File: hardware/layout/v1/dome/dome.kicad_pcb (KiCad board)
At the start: 4 copper layers, 13.6 x 13.6 mm, 5 parts, among them J1 CROWN_RISER, U1 LTR-390UV-01, U2 VEML7700-TT

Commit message: Update documentation to reflect hardware specification changes and component substitutions
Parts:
- moved C2 8.42 mm to (6.80, -2.10)
- moved C1 2.64 mm to (6.80, -11.5)
- moved J1 1.30 mm to (6.80, -6.80)
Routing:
- net I2C_SCL: track 8.54 -> 11.1 mm
- net I2C_SDA: track 11.5 -> 13.3 mm, vias 2 -> 1
- net GND: track 17.9 -> 16.3 mm
- net +3V3: track 20.0 -> 19.5 mm

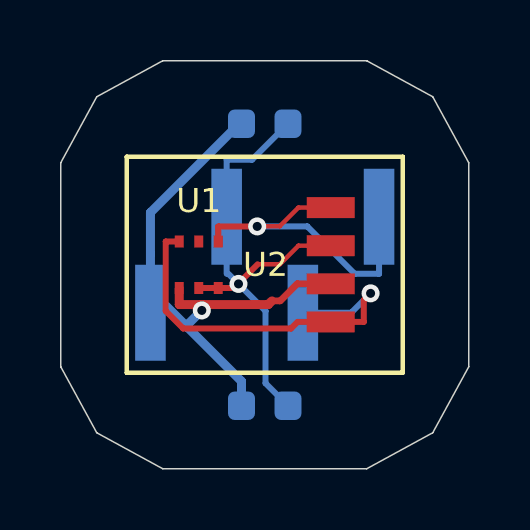
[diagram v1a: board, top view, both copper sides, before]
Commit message: Redesign crown PCB
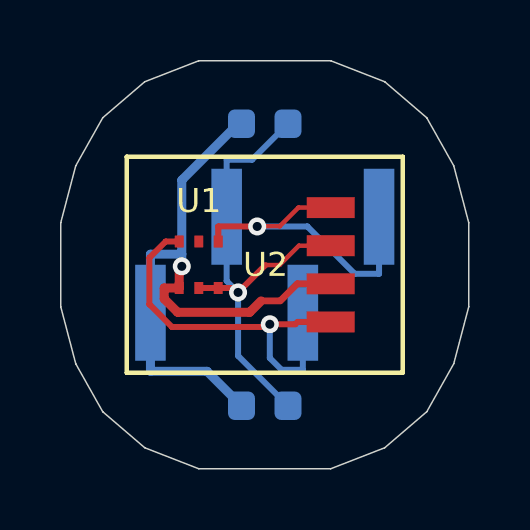
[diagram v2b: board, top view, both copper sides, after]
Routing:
- net +3V3: track 19.5 -> 21.9 mm
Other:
- outline, holes or cut-outs redrawn

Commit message: Add silkscreen connector labels to all PCB variants for improved assembly identification
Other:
- board text added: "CROWN"

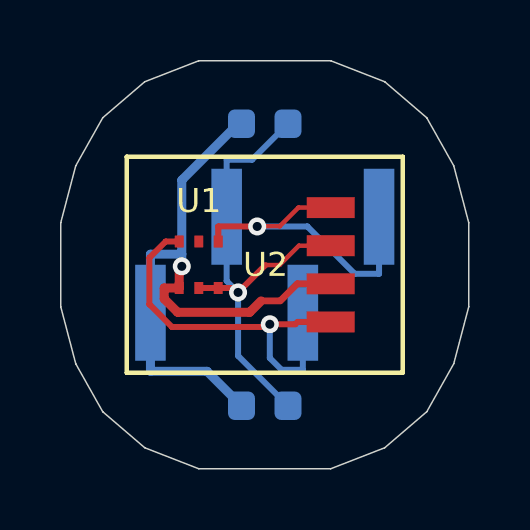
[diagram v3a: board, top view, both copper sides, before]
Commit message: Upgrade dome PCB with enhanced light sensing capabilities: add TSL25911FN visible/NIR sensor and optional GUVB-C31SM UV-B sensor
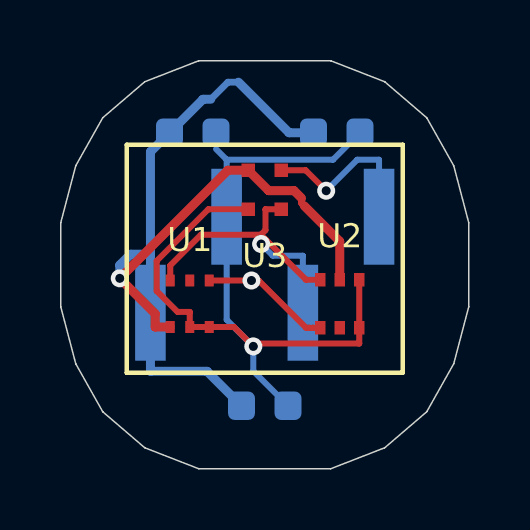
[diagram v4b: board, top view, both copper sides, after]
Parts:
- added C3: 100n 50V, Capacitor_SMD:C_0603_1608Metric, B.Cu at (6.80, -2.10)
- added U3: GUVB-C31SM, gateway_fp:GenUV_GUVB-C31SM, F.Cu at (6.80, -9.30)
- U2: value VEML7700-TT -> TSL25911FN; footprint gateway_fp:Vishay_VEML7700-TT -> gateway_fp:AMS_TSL25911FN
- moved C2 9.41 mm to (9.20, -11.2)
- moved C1 2.42 mm to (4.40, -11.2)
- moved U1 1.33 mm to (4.30, -5.50)
- moved U2 1.33 mm to (9.30, -5.50), turned to 0 degrees
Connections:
- U2 pad 1: I2C_SDA -> I2C_SCL
- U2 pad 2: +3V3 -> (no net)
- U2 pad 4: I2C_SCL -> GND
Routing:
- net GND: track 16.5 -> 29.0 mm
- net +3V3: track 21.9 -> 33.3 mm
- net I2C_SCL: track 11.1 -> 14.2 mm, vias 1 -> 2
- net I2C_SDA: track 13.5 -> 11.7 mm

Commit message: Update enclosure dimensions, add power board, upgrade sensors, and redesign base bay for PMSA003I particulate module
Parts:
- C3: value 100n 50V -> 1u 50V

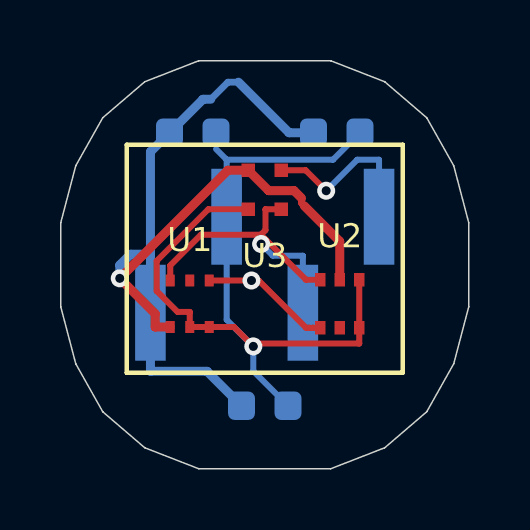
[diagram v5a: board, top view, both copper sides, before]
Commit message: Update documentation for 60V power system, STM32 crown board, 12V heaters, and expanded enclosure design
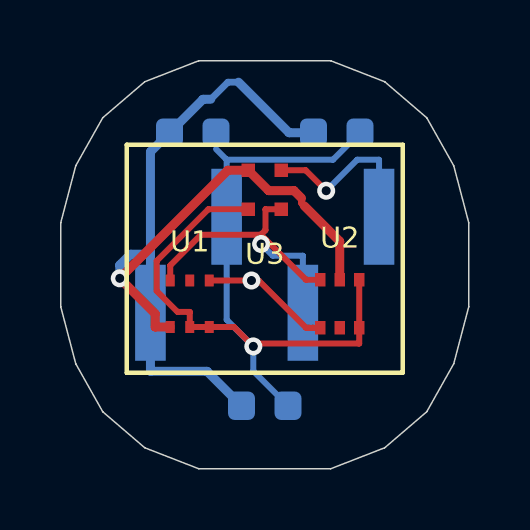
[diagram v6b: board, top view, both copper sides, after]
